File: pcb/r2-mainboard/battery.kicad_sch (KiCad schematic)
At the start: 35 parts, among them J1 USB-C 16P, J2 Pico-Lock 504050-0391, J25 SolderPads 3x, U1 BQ25892RTW, U2 MAX17048G+T10, U3 USBLC6-2SC6

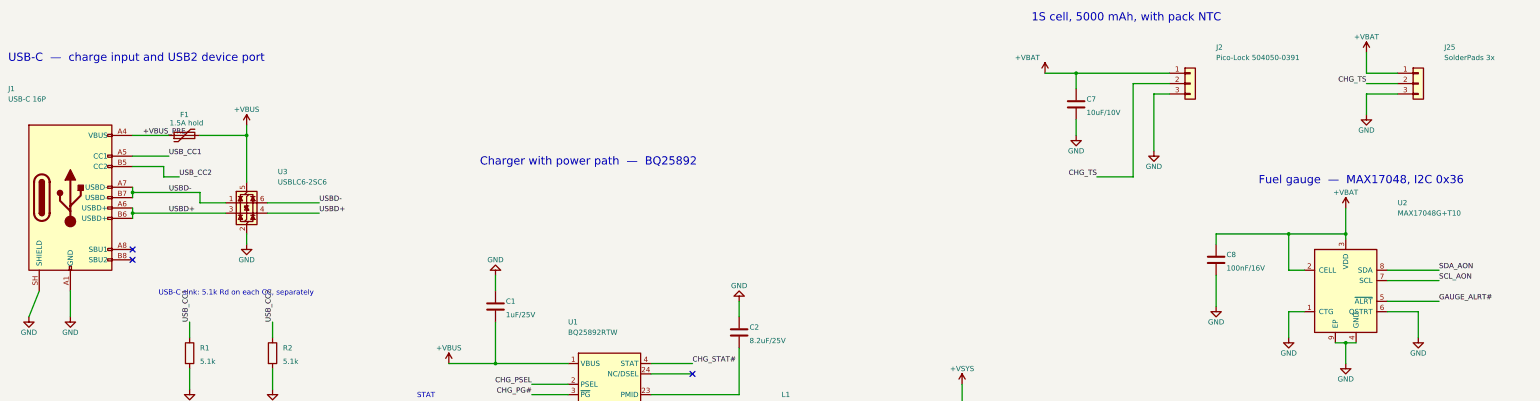
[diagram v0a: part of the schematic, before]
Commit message: Docs: library audit list and a first production costing
libraries.md -- every symbol in r2.kicad_sym and every footprint in
r2.pretty, with what it was derived from, which tools/ script emits it,
and what was actually checked. Written for the owner's audit before the
libraries get rehomed. Notes that pcb_common has never been modified,
and calls out the three newest entries (TPS2553DBV and the two
_Mirrored FPC land patterns) as the least reviewed.

NOTES-production-costing.md -- what 1000 units costs and what a campaign
would have to raise, prompted by Good Display's US$750 / MOQ 1000 quote.
Central estimate EUR 340/unit COGS and a EUR ~548k goal, but the honest
finding is the sensitivity: the PCM-071 at EUR 250 @1-9 costs more than
the display, and the sibling quote says ~EUR 190 of that is a memory-
shortage surcharge. A 1000-piece quote moves the goal by EUR 290k, so it
is the single highest-value thing to chase. Also states plainly that at
the central estimate the margin is thin to negative against market
comparables, and what to do about it.

Both indexed in CLAUDE.md.

Co-Authored-By: Claude Opus 5 <noreply@anthropic.com>
Claude-Session: https://claude.ai/code/session_01MHTAe6ZnhogTEgtyPcLhwG
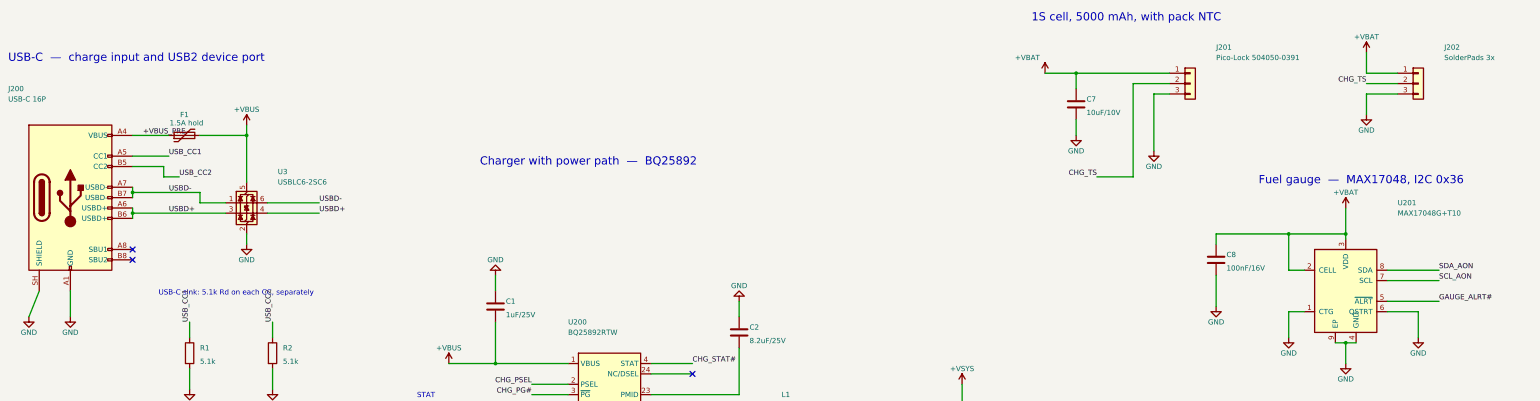
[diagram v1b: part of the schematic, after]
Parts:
- renumbered J1 to J200, J2 to J201, J25 to J202, U1 to U200, U2 to U201
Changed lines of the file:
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@@
 		(in_pos_files yes)
 		(dnp no)
-		(property "Reference" "U2"
+		(property "Reference" "U201"
 			(at 370.84 64.77 0)
 			(show_name no)
@@
 			(project "r2"
 				(path "/dee825bf-c2f1-415d-afdf-cf702072a6e8/a6dcf48c-d5d2-42bd-8aa1-b0910921d2ee"
-					(reference "U2")
+					(reference "U201")
 					(unit 1)
 				)
@@
 		(in_pos_files yes)
 		(dnp no)
-		(property "Reference" "U1"
+		(property "Reference" "U200"
 			(at 167.64 93.98 0)
 			(show_name no)
@@
 			(project "r2"
 				(path "/dee825bf-c2f1-415d-afdf-cf702072a6e8/a6dcf48c-d5d2-42bd-8aa1-b0910921d2ee"
-					(reference "U1")
+					(reference "U200")
 					(unit 1)
 				)
@@
 		(in_pos_files yes)
 		(dnp no)
-		(property "Reference" "J2"
+		(property "Reference" "J201"
 			(at 326.39 26.67 0)
 			(show_name no)
@@
 			(project "r2"
 				(path "/dee825bf-c2f1-415d-afdf-cf702072a6e8/a6dcf48c-d5d2-42bd-8aa1-b0910921d2ee"
-					(reference "J2")
+					(reference "J201")
 					(unit 1)
 				)
@@
 		(in_pos_files yes)
 		(dnp no)
-		(property "Reference" "J1"
+		(property "Reference" "J200"
 			(at 30.48 36.83 0)
 			(show_name no)
@@
 			(project "r2"
 				(path "/dee825bf-c2f1-415d-afdf-cf702072a6e8/a6dcf48c-d5d2-42bd-8aa1-b0910921d2ee"
-					(reference "J1")
+					(reference "J200")
 					(unit 1)
 				)
@@
 		(in_pos_files yes)
 		(dnp no)
-		(property "Reference" "J25"
+		(property "Reference" "J202"
 			(at 382.27 26.67 0)
 			(show_name no)
@@
 			(project "r2"
 				(path "/dee825bf-c2f1-415d-afdf-cf702072a6e8/a6dcf48c-d5d2-42bd-8aa1-b0910921d2ee"
-					(reference "J25")
+					(reference "J202")
 					(unit 1)
 				)

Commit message: R2: renumber every sheet to the page-based designator scheme
The owner's scheme is classifier + sheet page + two-digit part from 00. Four
sheets already used it; this converts the remaining nine, so all thirteen now
agree: pages 2-9 take three digits, pages 10-14 four. 292 of 333 designators
changed. A part shared by several sheets takes its lowest page, so the FPGA is
U700 (pages 7-9) and the two SoM connectors are J501/J502 (pages 5-6).

The whole risk here is silently rewiring the board, so the netlist was diffed
rather than eyeballed:

  nets 519 -> 519, total pin connections 1563 -> 1563
  named nets present in both whose pin multiset changed: 0
  ERC unchanged at 14 errors / 20 warnings
  check_ucf.py: 99 balls matched, 0 failures

That last one matters most: it resolves the gateware's 113 UCF constraints to
board nets *by ball name*, so it is the sharpest detector of the corruption
this change could cause.

Two earlier attempts did cause exactly that. A bare quoted-string substitution
also rewrites FPGA ball names (C1, D2, N11, T1) and BTH-060 pin names (A1-D60),
which are spelled exactly like designators; one run left ERC identical while 40
nets came back with a different pin multiset. The tool now substitutes only at
the two positions that store an instance's designator, and excludes every pin
name everywhere else. docs/layout.md 9.5 records the hazard and how to prove a
renumber was clean.

Only the three scripts that read the design are updated. The gen_*/patch_*/
port_r1.py scripts keep the old names deliberately: each wrote a sheet once and
has not been re-runnable since it was hand-edited in Eeschema, so they are a
historical record -- and port_r1.py's dict keys are R1 designators that were
never renumbered at all.

Co-Authored-By: Claude Opus 5 <noreply@anthropic.com>
Claude-Session: https://claude.ai/code/session_01MHTAe6ZnhogTEgtyPcLhwG
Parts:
- renumbered C1 to C200, C2 to C201, C3 to C202, C4 to C203, C5 to C204, C6 to C205, C7 to C206, C8 to C207, D7 to D200, F1 to F200, L1 to L200, R1 to R200, R2 to R201, R3 to R202, R4 to R203, R5 to R204, R6 to R205, R7 to R206, R8 to R207, R9 to R208, R10 to R209, R11 to R210, R12 to R211, R13 to R212, R17 to R213, R18 to R214, R19 to R215, R37 to R216, R38 to R217, U3 to U202
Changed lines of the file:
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@@
 		(in_pos_files yes)
 		(dnp no)
-		(property "Reference" "R4"
+		(property "Reference" "R203"
 			(at 130.81 176.53 0)
 			(show_name no)
@@
 			(project "r2"
 				(path "/dee825bf-c2f1-415d-afdf-cf702072a6e8/a6dcf48c-d5d2-42bd-8aa1-b0910921d2ee"
-					(reference "R4")
+					(reference "R203")
 					(unit 1)
 				)
@@
 		(in_pos_files yes)
 		(dnp no)
-		(property "Reference" "F1"
+		(property "Reference" "F200"
 			(at 73.66 43.18 270)
 			(show_name no)
@@
 			(project "r2"
 				(path "/dee825bf-c2f1-415d-afdf-cf702072a6e8/a6dcf48c-d5d2-42bd-8aa1-b0910921d2ee"
-					(reference "F1")
+					(reference "F200")
 					(unit 1)
 				)
@@
 		(in_pos_files yes)
 		(dnp no)
-		(property "Reference" "C5"
+		(property "Reference" "C204"
 			(at 254 125.73 0)
 			(show_name no)
@@
 			(project "r2"
 				(path "/dee825bf-c2f1-415d-afdf-cf702072a6e8/a6dcf48c-d5d2-42bd-8aa1-b0910921d2ee"
-					(reference "C5")
+					(reference "C204")
 					(unit 1)
 				)
@@
 		(in_pos_files yes)
 		(dnp no)
-		(property "Reference" "R1"
+		(property "Reference" "R200"
 			(at 77.47 100.33 0)
 			(show_name no)
@@
 			(project "r2"
 				(path "/dee825bf-c2f1-415d-afdf-cf702072a6e8/a6dcf48c-d5d2-42bd-8aa1-b0910921d2ee"
-					(reference "R1")
+					(reference "R200")
 					(unit 1)
 				)
@@
 		(in_pos_files yes)
 		(dnp no)
-		(property "Reference" "R9"
+		(property "Reference" "R208"
 			(at 223.52 167.64 0)
 			(show_name no)
@@
 			(project "r2"
 				(path "/dee825bf-c2f1-415d-afdf-cf702072a6e8/a6dcf48c-d5d2-42bd-8aa1-b0910921d2ee"
-					(reference "R9")
+					(reference "R208")
 					(unit 1)
 				)
@@
 		(in_pos_files yes)
 		(dnp no)
-		(property "Reference" "R5"
+		(property "Reference" "R204"
 			(at 151.13 176.53 0)
 			(show_name no)
@@
 			(project "r2"
 				(path "/dee825bf-c2f1-415d-afdf-cf702072a6e8/a6dcf48c-d5d2-42bd-8aa1-b0910921d2ee"
-					(reference "R5")
+					(reference "R204")
 					(unit 1)
 				)
@@
 		(in_pos_files yes)
 		(dnp no)
-		(property "Reference" "C7"
+		(property "Reference" "C206"
 			(at 294.64 39.37 0)
 			(show_name no)
@@
 			(project "r2"
 				(path "/dee825bf-c2f1-415d-afdf-cf702072a6e8/a6dcf48c-d5d2-42bd-8aa1-b0910921d2ee"
-					(reference "C7")
+					(reference "C206")
 					(unit 1)
 				)
@@
 		(in_pos_files yes)
 		(dnp no)
-		(property "Reference" "C1"
+		(property "Reference" "C200"
 			(at 152.4 88.9 0)
 			(show_name no)
@@
 			(project "r2"
 				(path "/dee825bf-c2f1-415d-afdf-cf702072a6e8/a6dcf48c-d5d2-42bd-8aa1-b0910921d2ee"
-					(reference "C1")
+					(reference "C200")
 					(unit 1)
 				)
@@
 		(in_pos_files yes)
 		(dnp no)
-		(property "Reference" "C4"
+		(property "Reference" "C203"
 			(at 238.76 125.73 0)
 			(show_name no)
@@
 			(project "r2"
 				(path "/dee825bf-c2f1-415d-afdf-cf702072a6e8/a6dcf48c-d5d2-42bd-8aa1-b0910921d2ee"
-					(reference "C4")
+					(reference "C203")
 					(unit 1)
 				)
@@
 		(dnp no)
 		(fields_autoplaced yes)
-		(property "Reference" "R37"
+		(property "Reference" "R216"
 			(at 210.82 224.7899 0)
 			(show_name no)
@@
 			(project "r2"
 				(path "/dee825bf-c2f1-415d-afdf-cf702072a6e8/a6dcf48c-d5d2-42bd-8aa1-b0910921d2ee"
-					(reference "R37")
+					(reference "R216")
 					(unit 1)
 				)
@@
 		(in_pos_files yes)
 		(dnp no)
-		(property "Reference" "R18"
+		(property "Reference" "R214"
 			(at 129.54 204.47 0)
 			(show_name no)
@@
 			(project "r2"
 				(path "/dee825bf-c2f1-415d-afdf-cf702072a6e8/a6dcf48c-d5d2-42bd-8aa1-b0910921d2ee"
-					(reference "R18")
+					(reference "R214")
 					(unit 1)
 				)
@@
 		(in_pos_files yes)
 		(dnp no)
-		(property "Reference" "R13"
+		(property "Reference" "R212"
 			(at 375.92 148.59 0)
 			(show_name no)
@@
 			(project "r2"
 				(path "/dee825bf-c2f1-415d-afdf-cf702072a6e8/a6dcf48c-d5d2-42bd-8aa1-b0910921d2ee"
-					(reference "R13")
+					(reference "R212")
 					(unit 1)
 				)
@@
 		(in_pos_files yes)
 		(dnp no)
-		(property "Reference" "R10"
+		(property "Reference" "R209"
 			(at 223.52 181.61 0)
 			(show_name no)
@@
 			(project "r2"
 				(path "/dee825bf-c2f1-415d-afdf-cf702072a6e8/a6dcf48c-d5d2-42bd-8aa1-b0910921d2ee"
-					(reference "R10")
+					(reference "R209")
 					(unit 1)
 				)
@@
 		(in_pos_files yes)
 		(dnp no)
-		(property "Reference" "L1"
+		(property "Reference" "L200"
 			(at 220.98 111.76 270)
 			(show_name no)
@@
 			(project "r2"
 				(path "/dee825bf-c2f1-415d-afdf-cf702072a6e8/a6dcf48c-d5d2-42bd-8aa1-b0910921d2ee"
-					(reference "L1")
+					(reference "L200")
 					(unit 1)
 				)
@@
 		(in_pos_files yes)
 		(dnp no)
-		(property "Reference" "U3"
+		(property "Reference" "U202"
 			(at 96.52 57.15 0)
 			(show_name no)
@@
 			(project "r2"
 				(path "/dee825bf-c2f1-415d-afdf-cf702072a6e8/a6dcf48c-d5d2-42bd-8aa1-b0910921d2ee"
-					(reference "U3")
+					(reference "U202")
 					(unit 1)
 				)
@@
 		(in_pos_files yes)
 		(dnp no)
-		(property "Reference" "R3"
+		(property "Reference" "R202"
 			(at 110.49 176.53 0)
 			(show_name no)
@@
 			(project "r2"
 				(path "/dee825bf-c2f1-415d-afdf-cf702072a6e8/a6dcf48c-d5d2-42bd-8aa1-b0910921d2ee"
-					(reference "R3")
+					(reference "R202")
 					(unit 1)
 				)
@@
 		(in_pos_files yes)
 		(dnp yes)
-		(property "Reference" "R11"
+		(property "Reference" "R210"
 			(at 341.63 134.62 0)
 			(show_name no)
@@
 			(project "r2"
 				(path "/dee825bf-c2f1-415d-afdf-cf702072a6e8/a6dcf48c-d5d2-42bd-8aa1-b0910921d2ee"
-					(reference "R11")
+					(reference "R210")
 					(unit 1)
 				)
@@
 		(in_pos_files yes)
 		(dnp no)
-		(property "Reference" "C8"
+		(property "Reference" "C207"
 			(at 328.93 77.47 0)
 			(show_name no)
@@
 			(project "r2"
 				(path "/dee825bf-c2f1-415d-afdf-cf702072a6e8/a6dcf48c-d5d2-42bd-8aa1-b0910921d2ee"
-					(reference "C8")
+					(reference "C207")
 					(unit 1)
 				)
@@
 		(in_pos_files yes)
 		(dnp no)
-		(property "Reference" "R2"
+		(property "Reference" "R201"
 			(at 97.79 100.33 0)
 			(show_name no)
@@
 			(project "r2"
 				(path "/dee825bf-c2f1-415d-afdf-cf702072a6e8/a6dcf48c-d5d2-42bd-8aa1-b0910921d2ee"
-					(reference "R2")
+					(reference "R201")
 					(unit 1)
 				)
@@
 		(in_pos_files yes)
 		(dnp no)
-		(property "Reference" "R12"
+		(property "Reference" "R211"
 			(at 375.92 134.62 0)
 			(show_name no)
@@
 			(project "r2"
 				(path "/dee825bf-c2f1-415d-afdf-cf702072a6e8/a6dcf48c-d5d2-42bd-8aa1-b0910921d2ee"
-					(reference "R12")
+					(reference "R211")
 					(unit 1)
 				)
@@
 		(in_pos_files yes)
 		(dnp no)
-		(property "Reference" "C3"
+		(property "Reference" "C202"
 			(at 202.438 119.888 270)
 			(show_name no)
@@
 			(project "r2"
 				(path "/dee825bf-c2f1-415d-afdf-cf702072a6e8/a6dcf48c-d5d2-42bd-8aa1-b0910921d2ee"
-					(reference "C3")
+					(reference "C202")
 					(unit 1)
 				)
@@
 		(in_pos_files yes)
 		(dnp no)
-		(property "Reference" "C6"
+		(property "Reference" "C205"
 			(at 217.17 142.24 0)
 			(show_name no)
@@
 			(project "r2"
 				(path "/dee825bf-c2f1-415d-afdf-cf702072a6e8/a6dcf48c-d5d2-42bd-8aa1-b0910921d2ee"
-					(reference "C6")
+					(reference "C205")
 					(unit 1)
 				)
@@
 		(in_pos_files yes)
 		(dnp no)
-		(property "Reference" "R8"
+		(property "Reference" "R207"
 			(at 161.29 142.24 0)
 			(show_name no)
@@
 			(project "r2"
 				(path "/dee825bf-c2f1-415d-afdf-cf702072a6e8/a6dcf48c-d5d2-42bd-8aa1-b0910921d2ee"
-					(reference "R8")
+					(reference "R207")
 					(unit 1)
 				)
@@
 		(in_pos_files yes)
 		(dnp no)
-		(property "Reference" "R7"
+		(property "Reference" "R206"
 			(at 191.77 176.53 0)
 			(show_name no)
@@
 			(project "r2"
 				(path "/dee825bf-c2f1-415d-afdf-cf702072a6e8/a6dcf48c-d5d2-42bd-8aa1-b0910921d2ee"
-					(reference "R7")
+					(reference "R206")
 					(unit 1)
 				)
@@
 		(in_pos_files yes)
 		(dnp no)
-		(property "Reference" "C2"
+		(property "Reference" "C201"
 			(at 212.09 95.25 0)
 			(show_name no)
@@
 			(project "r2"
 				(path "/dee825bf-c2f1-415d-afdf-cf702072a6e8/a6dcf48c-d5d2-42bd-8aa1-b0910921d2ee"
-					(reference "C2")
+					(reference "C201")
 					(unit 1)
 				)
@@
 		(in_pos_files yes)
 		(dnp no)
-		(property "Reference" "R19"
+		(property "Reference" "R215"
 			(at 325.12 134.62 0)
 			(show_name no)
@@
 			(project "r2"
 				(path "/dee825bf-c2f1-415d-afdf-cf702072a6e8/a6dcf48c-d5d2-42bd-8aa1-b0910921d2ee"
-					(reference "R19")
+					(reference "R215")
 					(unit 1)
 				)
@@
 		(in_pos_files yes)
 		(dnp no)
-		(property "Reference" "R17"
+		(property "Reference" "R213"
 			(at 109.22 204.47 0)
 			(show_name no)
@@
 			(project "r2"
 				(path "/dee825bf-c2f1-415d-afdf-cf702072a6e8/a6dcf48c-d5d2-42bd-8aa1-b0910921d2ee"
-					(reference "R17")
+					(reference "R213")
 					(unit 1)
 				)
@@
 		(dnp no)
 		(fields_autoplaced yes)
-		(property "Reference" "D7"
+		(property "Reference" "D200"
 			(at 212.09 233.9974 90)
 			(show_name no)
@@
 			(project "r2"
 				(path "/dee825bf-c2f1-415d-afdf-cf702072a6e8/a6dcf48c-d5d2-42bd-8aa1-b0910921d2ee"
-					(reference "D7")
+					(reference "D200")
 					(unit 1)
 				)
@@
 		(in_pos_files yes)
 		(dnp no)
-		(property "Reference" "R38"
+		(property "Reference" "R217"
 			(at 361.95 134.62 0)
 			(show_name no)
@@
 			(project "r2"
 				(path "/dee825bf-c2f1-415d-afdf-cf702072a6e8/a6dcf48c-d5d2-42bd-8aa1-b0910921d2ee"
-					(reference "R38")
+					(reference "R217")
 					(unit 1)
 				)
@@
 		(in_pos_files yes)
 		(dnp no)
-		(property "Reference" "R6"
+		(property "Reference" "R205"
 			(at 171.45 176.53 0)
 			(show_name no)
@@
 			(project "r2"
 				(path "/dee825bf-c2f1-415d-afdf-cf702072a6e8/a6dcf48c-d5d2-42bd-8aa1-b0910921d2ee"
-					(reference "R6")
+					(reference "R205")
 					(unit 1)
 				)
